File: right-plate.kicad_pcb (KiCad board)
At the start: 2 copper layers, 207.7 x 113.1 mm, 42 parts

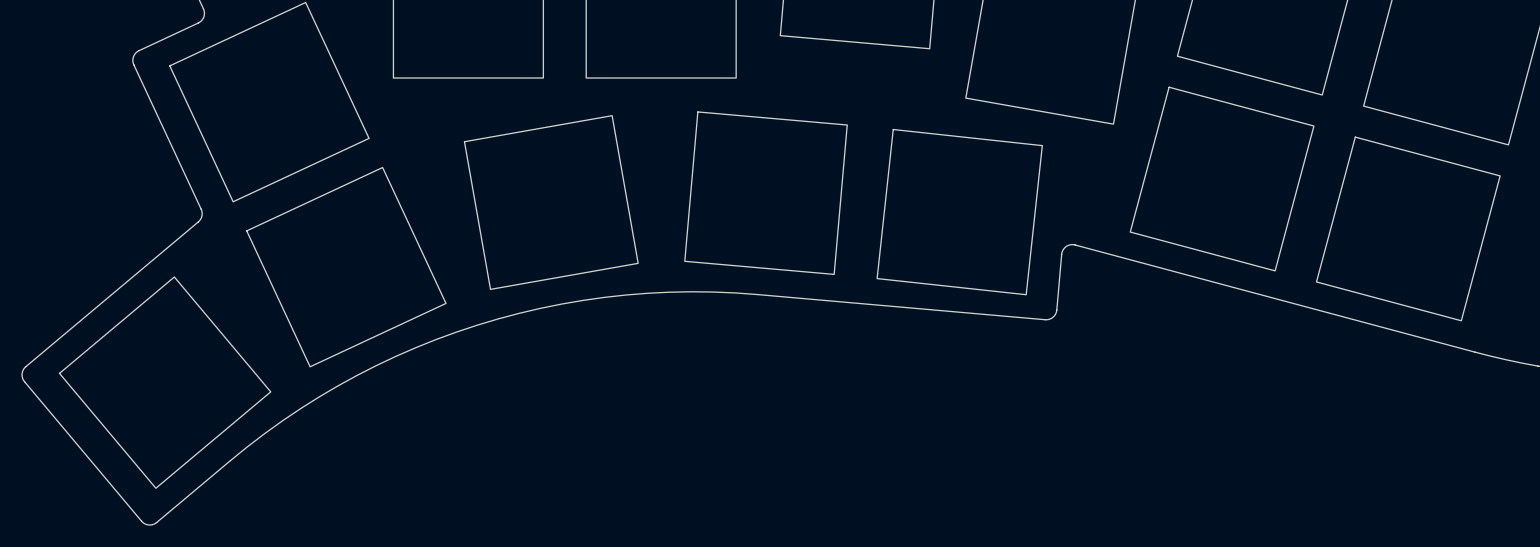
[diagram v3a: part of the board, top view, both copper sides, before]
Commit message: remove two thumb keys
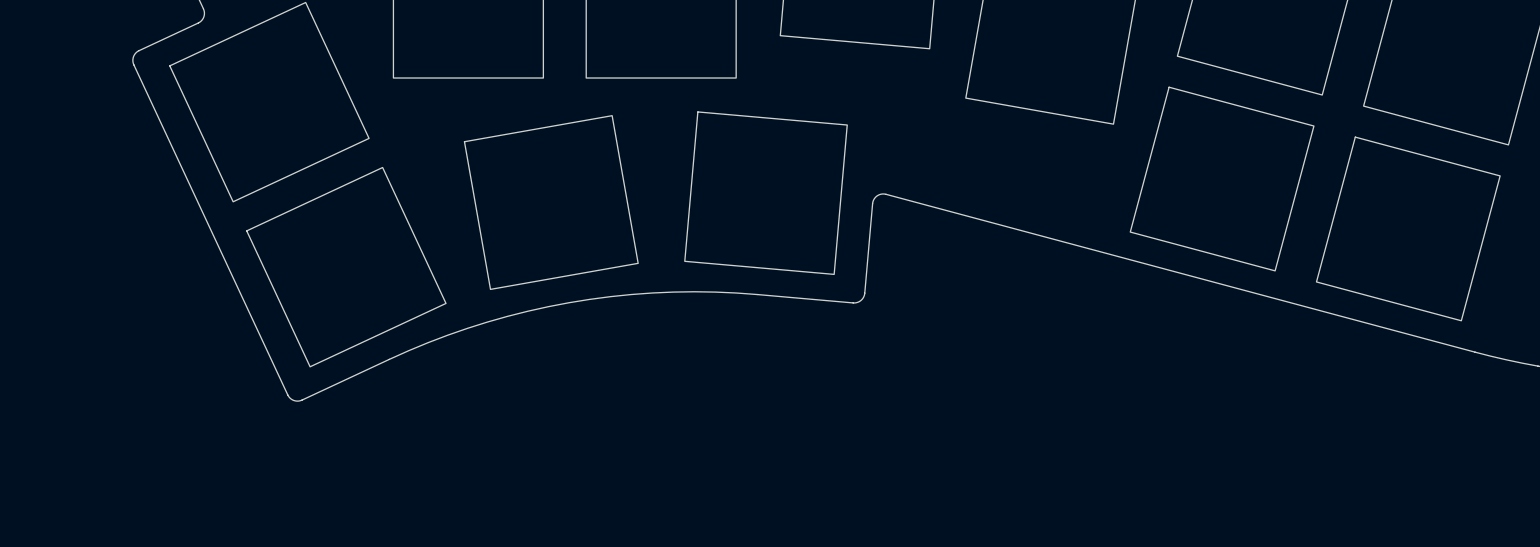
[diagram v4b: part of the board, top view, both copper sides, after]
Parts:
- removed the REF** at (125.7, 113.0)
- removed the REF** at (51.5, 128.9)
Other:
- board size 207.7 x 113.1 mm -> 197.4 x 107.7 mm
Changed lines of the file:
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@@
-  )
-  (footprint "keyboard:KeyHole" (layer "F.Cu")
-    (at 125.654248 113.020897 -6.171)
-    (fp_text reference "REF**" (at 0 0 -6.171 unlocked) (layer "F.Fab") hide
-      (effects (font (size 1 1) (thickness 0.1)))
-    )
-    (fp_text value "KeyHole" (at 0 2 -6.171 unlocked) (layer "F.Fab") hide
-      (effects (font (size 1 1) (thickness 0.125)))
-    )
-    (fp_rect (start -7 -7) (end 7 7) (layer "Edge.Cuts") (stroke (width 0.12) (type default)) (fill none))
   )
   (footprint "keyboard:KeyHole" (layer "F.Cu")
@@
   )
   (footprint "keyboard:KeyHole" (layer "F.Cu")
-    (at 51.462952 128.941816 40)
-    (fp_text reference "REF**" (at 0 0 40 unlocked) (layer "F.Fab") hide
-      (effects (font (size 1 1) (thickness 0.1)))
-    )
-    (fp_text value "KeyHole" (at 0 2 40 unlocked) (layer "F.Fab") hide
-      (effects (font (size 1 1) (thickness 0.125)))
-    )
-    (fp_rect (start -7 -7) (end 7 7) (layer "Edge.Cuts") (stroke (width 0.12) (type default)) (fill none))
-  )
-  (footprint "keyboard:KeyHole" (layer "F.Cu")
     (at 196.067849 86.124512 -10)
     (fp_text reference "REF**" (at 0 0 -10 unlocked) (layer "F.Fab") hide
@@
   )
   (gr_line (start 51.498654 86.442618) (end 55.041575 94.040436) (layer "Edge.Cuts") (width 0.12))
-  (gr_line (start 48.545718 99.276259) (end 54.828214 112.749115) (layer "Edge.Cuts") (width 0.12))
+  (gr_line (start 48.545718 99.276259) (end 62.914739 130.090724) (layer "Edge.Cuts") (width 0.12))
   (gr_line (start 144.838586 37.117093) (end 153.701856 38.679926) (layer "Edge.Cuts") (width 0.12))
   (gr_line (start 179.650884 127.400816) (end 232.830502 136.777818) (layer "Edge.Cuts") (width 0.12))
@@
   (gr_line (start 70.78 33) (end 97.78 33) (layer "Edge.Cuts") (width 0.12))
   (gr_arc (start 132.2977 35.20728) (mid 131.646186 34.842587) (end 131.42888 34.128269) (layer "Edge.Cuts") (width 0.12))
+  (gr_arc (start 117.519499 112.23964) (mid 117.942117 111.507644) (end 118.774513 111.36087) (layer "Edge.Cuts") (width 0.12))
   (gr_arc (start 153.945198 48.315494) (mid 153.360626 47.886868) (end 153.219209 47.17592) (layer "Edge.Cuts") (width 0.12))
   (gr_arc (start 153.701856 38.679926) (mid 154.34736 39.091158) (end 154.513015 39.838382) (layer "Edge.Cuts") (width 0.12))
-  (gr_line (start 54.564694 113.937777) (end 38.462071 127.449483) (layer "Edge.Cuts") (width 0.12))
-  (gr_arc (start 57.569435 136.219239) (mid 80.612677 123.577284) (end 106.739723 120.715907) (layer "Edge.Cuts") (width 0.12))
   (gr_line (start 131.42888 34.128269) (end 131.63429 31.780424) (layer "Edge.Cuts") (width 0.12))
   (gr_line (start 68.78 85.02) (end 52.404962 85.02) (layer "Edge.Cuts") (width 0.12))
   (gr_line (start 191.80707 58.460552) (end 153.945198 48.315494) (layer "Edge.Cuts") (width 0.12))
-  (gr_arc (start 50.675034 142.004326) (mid 49.945092 142.234476) (end 49.266203 141.88107) (layer "Edge.Cuts") (width 0.12))
-  (gr_arc (start 54.828214 112.749115) (mid 54.898202 113.388172) (end 54.564694 113.937777) (layer "Edge.Cuts") (width 0.12))
   (gr_arc (start 48.545718 99.276259) (mid 48.512334 98.511621) (end 49.029408 97.947333) (layer "Edge.Cuts") (width 0.12))
-  (gr_line (start 135.17438 116.970262) (end 134.720331 122.160072) (layer "Edge.Cuts") (width 0.12))
   (gr_arc (start 233.988959 135.966658) (mid 233.577727 136.612162) (end 232.830502 136.777818) (layer "Edge.Cuts") (width 0.12))
   (gr_arc (start 97.78 33) (mid 104.122734 33.074236) (end 110.461994 33.296903) (layer "Edge.Cuts") (width 0.12))
   (gr_line (start 54.557885 95.369362) (end 49.029408 97.947333) (layer "Edge.Cuts") (width 0.12))
-  (gr_line (start 173.774094 126.097962) (end 136.429395 116.091481) (layer "Edge.Cuts") (width 0.12))
-  (gr_arc (start 134.720331 122.160072) (mid 134.366924 122.838961) (end 133.63698 123.069112) (layer "Edge.Cuts") (width 0.12))
+  (gr_line (start 173.774094 126.097962) (end 118.774513 111.36087) (layer "Edge.Cuts") (width 0.12))
   (gr_arc (start 130.725251 30.697074) (mid 131.40414 31.050481) (end 131.63429 31.780424) (layer "Edge.Cuts") (width 0.12))
-  (gr_line (start 133.63698 123.069111) (end 106.739723 120.715906) (layer "Edge.Cuts") (width 0.12))
+  (gr_arc (start 72.400435 126.770849) (mid 89.171515 121.482952) (end 106.739743 120.715908) (layer "Edge.Cuts") (width 0.12))
   (gr_line (start 111.710396 30.037309) (end 111.504986 32.385154) (layer "Edge.Cuts") (width 0.12))
-  (gr_arc (start 38.338814 128.858315) (mid 38.108663 128.128371) (end 38.462071 127.449482) (layer "Edge.Cuts") (width 0.12))
+  (gr_line (start 116.788826 120.591269) (end 117.519499 112.23964) (layer "Edge.Cuts") (width 0.12))
   (gr_arc (start 111.504986 32.385154) (mid 111.16694 33.050886) (end 110.461994 33.296902) (layer "Edge.Cuts") (width 0.12))
   (gr_line (start 69.78 84.02) (end 69.78 34) (layer "Edge.Cuts") (width 0.12))
-  (gr_line (start 50.675034 142.004326) (end 57.569435 136.219239) (layer "Edge.Cuts") (width 0.12))
   (gr_arc (start 51.498654 86.442618) (mid 51.56157 85.4827) (end 52.404962 85.02) (layer "Edge.Cuts") (width 0.12))
   (gr_line (start 191.892252 58.479437) (end 244.985875 67.841276) (layer "Edge.Cuts") (width 0.12))
   (gr_arc (start 69.78 84.02) (mid 69.487107 84.727107) (end 68.78 85.02) (layer "Edge.Cuts") (width 0.12))
   (gr_arc (start 69.78 34) (mid 70.072893 33.292893) (end 70.78 33) (layer "Edge.Cuts") (width 0.12))
+  (gr_arc (start 116.788826 120.591269) (mid 116.435419 121.270158) (end 115.705476 121.500308) (layer "Edge.Cuts") (width 0.12))
   (gr_arc (start 132.2977 35.20728) (mid 138.579319 36.088797) (end 144.838586 37.117094) (layer "Edge.Cuts") (width 0.12))
-  (gr_line (start 49.266202 141.88107) (end 38.338813 128.858315) (layer "Edge.Cuts") (width 0.12))
   (gr_arc (start 179.650884 127.400815) (mid 176.698275 126.813504) (end 173.774094 126.097962) (layer "Edge.Cuts") (width 0.12))
   (gr_line (start 154.513015 39.838382) (end 153.219209 47.17592) (layer "Edge.Cuts") (width 0.12))
-  (gr_arc (start 135.17438 116.970262) (mid 135.596995 116.238258) (end 136.429395 116.091481) (layer "Edge.Cuts") (width 0.12))
+  (gr_line (start 115.705476 121.500308) (end 106.739743 120.715908) (layer "Edge.Cuts") (width 0.12))
+  (gr_arc (start 64.243674 130.57441) (mid 63.479031 130.6078) (end 62.914739 130.090724) (layer "Edge.Cuts") (width 0.12))
   (gr_arc (start 55.041575 94.040436) (mid 55.074959 94.805074) (end 54.557885 95.369362) (layer "Edge.Cuts") (width 0.12))
   (gr_line (start 130.725251 30.697074) (end 112.793746 29.12827) (layer "Edge.Cuts") (width 0.12))
   (gr_line (start 233.988959 135.966658) (end 245.797034 68.999731) (layer "Edge.Cuts") (width 0.12))
+  (gr_line (start 64.243674 130.574409) (end 72.400435 126.770849) (layer "Edge.Cuts") (width 0.12))
 )

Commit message: remove area under palm
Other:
- outline, holes or cut-outs redrawn
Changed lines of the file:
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@@
   )
   (gr_line (start 51.498654 86.442618) (end 55.041575 94.040436) (layer "Edge.Cuts") (width 0.12))
+  (gr_arc (start 119.250898 104.150057) (mid 125.98312 104.988487) (end 132.683213 106.053635) (layer "Edge.Cuts") (width 0.12))
   (gr_line (start 48.545718 99.276259) (end 62.914739 130.090724) (layer "Edge.Cuts") (width 0.12))
   (gr_line (start 144.838586 37.117093) (end 153.701856 38.679926) (layer "Edge.Cuts") (width 0.12))
   (gr_line (start 179.650884 127.400816) (end 232.830502 136.777818) (layer "Edge.Cuts") (width 0.12))
   (gr_arc (start 244.985875 67.841276) (mid 245.631378 68.252507) (end 245.797034 68.999731) (layer "Edge.Cuts") (width 0.12))
+  (gr_line (start 132.683213 106.053635) (end 139.397025 107.237462) (layer "Edge.Cuts") (width 0.12))
   (gr_arc (start 111.710396 30.037309) (mid 112.063803 29.35842) (end 112.793746 29.12827) (layer "Edge.Cuts") (width 0.12))
   (gr_arc (start 191.892252 58.479437) (mid 191.849455 58.470924) (end 191.80707 58.460552) (layer "Edge.Cuts") (width 0.12))
+  (gr_arc (start 139.000764 116.780478) (mid 138.393558 116.314552) (end 138.293657 115.555733) (layer "Edge.Cuts") (width 0.12))
   (gr_line (start 70.78 33) (end 97.78 33) (layer "Edge.Cuts") (width 0.12))
   (gr_arc (start 132.2977 35.20728) (mid 131.646186 34.842587) (end 131.42888 34.128269) (layer "Edge.Cuts") (width 0.12))
-  (gr_arc (start 117.519499 112.23964) (mid 117.942117 111.507644) (end 118.774513 111.36087) (layer "Edge.Cuts") (width 0.12))
   (gr_arc (start 153.945198 48.315494) (mid 153.360626 47.886868) (end 153.219209 47.17592) (layer "Edge.Cuts") (width 0.12))
   (gr_arc (start 153.701856 38.679926) (mid 154.34736 39.091158) (end 154.513015 39.838382) (layer "Edge.Cuts") (width 0.12))
@@
   (gr_arc (start 97.78 33) (mid 104.122734 33.074236) (end 110.461994 33.296903) (layer "Edge.Cuts") (width 0.12))
   (gr_line (start 54.557885 95.369362) (end 49.029408 97.947333) (layer "Edge.Cuts") (width 0.12))
-  (gr_line (start 173.774094 126.097962) (end 118.774513 111.36087) (layer "Edge.Cuts") (width 0.12))
+  (gr_arc (start 139.397025 107.237462) (mid 140.066768 107.68497) (end 140.189302 108.481088) (layer "Edge.Cuts") (width 0.12))
   (gr_arc (start 130.725251 30.697074) (mid 131.40414 31.050481) (end 131.63429 31.780424) (layer "Edge.Cuts") (width 0.12))
+  (gr_line (start 139.000764 116.780478) (end 173.774094 126.097962) (layer "Edge.Cuts") (width 0.12))
   (gr_arc (start 72.400435 126.770849) (mid 89.171515 121.482952) (end 106.739743 120.715908) (layer "Edge.Cuts") (width 0.12))
   (gr_line (start 111.710396 30.037309) (end 111.504986 32.385154) (layer "Edge.Cuts") (width 0.12))
-  (gr_line (start 116.788826 120.591269) (end 117.519499 112.23964) (layer "Edge.Cuts") (width 0.12))
+  (gr_line (start 116.788826 120.591269) (end 118.147883 105.05718) (layer "Edge.Cuts") (width 0.12))
   (gr_arc (start 111.504986 32.385154) (mid 111.16694 33.050886) (end 110.461994 33.296902) (layer "Edge.Cuts") (width 0.12))
   (gr_line (start 69.78 84.02) (end 69.78 34) (layer "Edge.Cuts") (width 0.12))
@@
   (gr_arc (start 116.788826 120.591269) (mid 116.435419 121.270158) (end 115.705476 121.500308) (layer "Edge.Cuts") (width 0.12))
   (gr_arc (start 132.2977 35.20728) (mid 138.579319 36.088797) (end 144.838586 37.117094) (layer "Edge.Cuts") (width 0.12))
+  (gr_arc (start 118.147883 105.05718) (mid 118.508889 104.37198) (end 119.250898 104.150059) (layer "Edge.Cuts") (width 0.12))
   (gr_arc (start 179.650884 127.400815) (mid 176.698275 126.813504) (end 173.774094 126.097962) (layer "Edge.Cuts") (width 0.12))
   (gr_line (start 154.513015 39.838382) (end 153.219209 47.17592) (layer "Edge.Cuts") (width 0.12))
   (gr_line (start 115.705476 121.500308) (end 106.739743 120.715908) (layer "Edge.Cuts") (width 0.12))
+  (gr_line (start 140.189303 108.481088) (end 138.293657 115.555733) (layer "Edge.Cuts") (width 0.12))
   (gr_arc (start 64.243674 130.57441) (mid 63.479031 130.6078) (end 62.914739 130.090724) (layer "Edge.Cuts") (width 0.12))
   (gr_arc (start 55.041575 94.040436) (mid 55.074959 94.805074) (end 54.557885 95.369362) (layer "Edge.Cuts") (width 0.12))
